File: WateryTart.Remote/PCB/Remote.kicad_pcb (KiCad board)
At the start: 2 copper layers, 41.3 x 112.4 mm, 26 parts, among them J1 Conn_01x04, J2 Conn_01x06, SW1 SW_Push, U1 lolin32_lite_V1.00

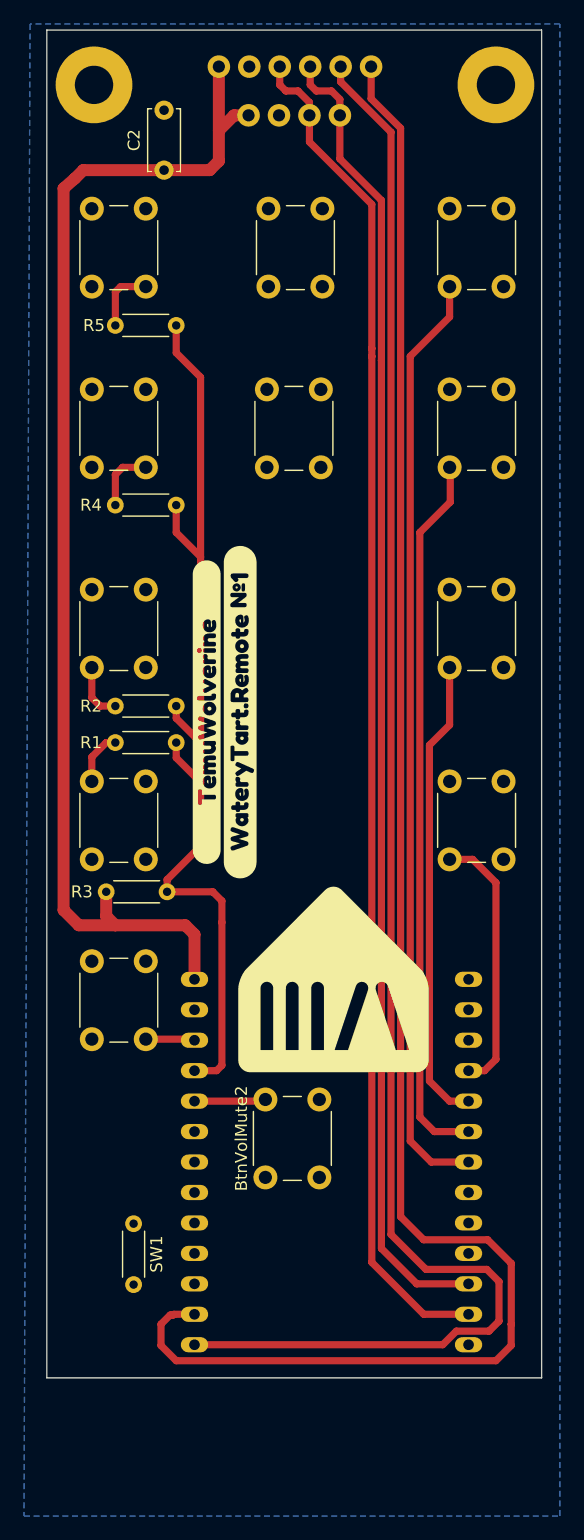
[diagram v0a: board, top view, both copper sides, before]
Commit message: Finalised schematic and pcb layout ready for first round of mfg
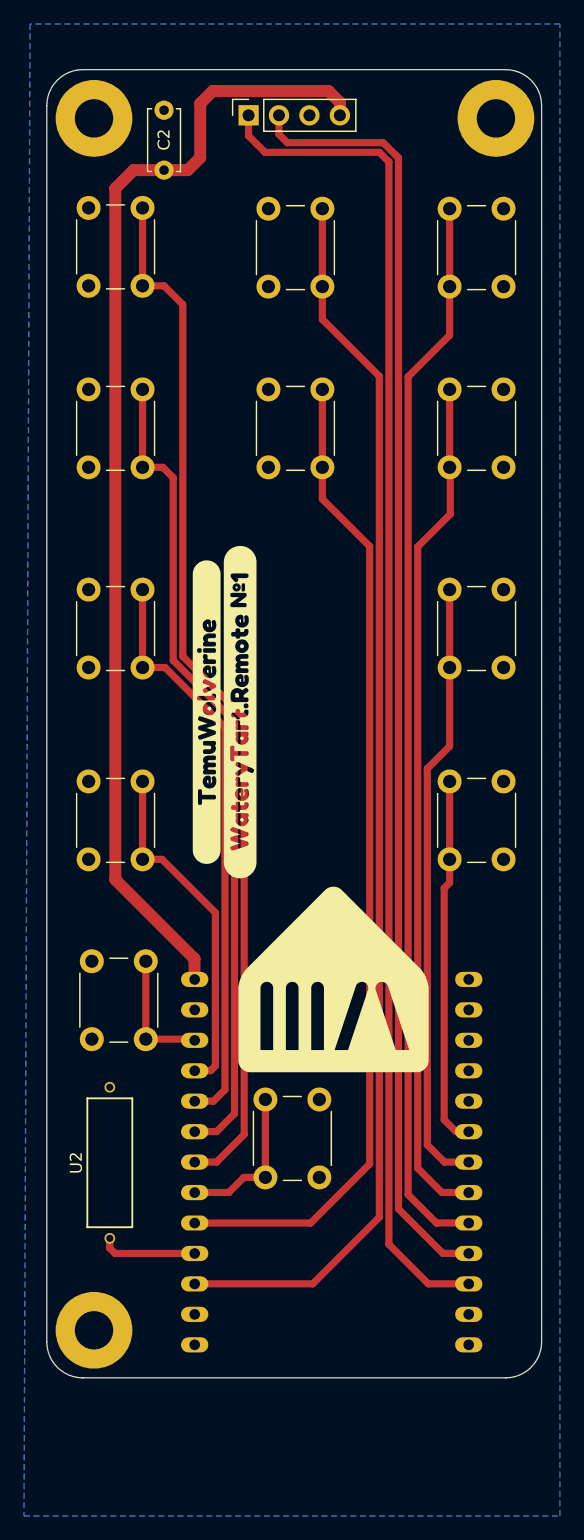
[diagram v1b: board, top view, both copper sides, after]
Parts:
- removed J2: Conn_01x06, PCM_SparkFun-Connector:1x06_P2.54mm
- removed R1: 220, Resistor_THT:R_Axial_DIN0204_L3.6mm_D1.6mm_P5.08mm_Horizontal
- removed R2: 4.7k, Resistor_THT:R_Axial_DIN0204_L3.6mm_D1.6mm_P5.08mm_Horizontal
- removed R3, R4: 10k, Resistor_THT:R_Axial_DIN0204_L3.6mm_D1.6mm_P5.08mm_Horizontal
- removed R5: 47k, Resistor_THT:R_Axial_DIN0204_L3.6mm_D1.6mm_P5.08mm_Horizontal
- removed SW1: SW_Push, Resistor_THT:R_Axial_DIN0204_L3.6mm_D1.6mm_P5.08mm_Horizontal
- added H3: MountingHole, MountingHole:MountingHole_3.2mm_M3_Pad, F.Cu at (122.7, 139.4)
- added U2: ~, EasyEDA_Lib:SW-TH_BD3.6-L10.6-LS12.6-D0.4, F.Cu at (124.0, 125.5)
- J1: footprint PCM_SparkFun-Connector:1x04_P2.54mm -> Connector_PinSocket_2.54mm:PinSocket_1x04_P2.54mm_Vertical
- U1: footprint PaulsCoolKicadLibrary:WEMOS_LOLIN32_LITE -> Paul:WEMOS_LOLIN32_LITE
- moved BtnVolDown1 8.06 mm to (122.2, 100.2), turned to 90 degrees
- moved BtnVolUp1 8.06 mm to (122.2, 84.2), turned to 90 degrees
- moved BtnPreviousTrack1 7.81 mm to (126.7, 45.8), turned to -90 degrees
- moved BtnCycleRepeat1 7.76 mm to (126.7, 61.0), turned to -90 degrees
- moved H1 2.79 mm to (122.7, 38.4)
- moved H2 2.79 mm to (156.2, 38.4)
- moved BtnFavourite1 0.13 mm to (137.2, 67.5)
- turned J1 to 90 degrees
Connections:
- BtnCycleRepeat1 pad 1: GND -> repeat
- BtnCycleRepeat1 pad 2: /sRepeat -> GND
- BtnPreviousTrack1 pad 1: GND -> previoustrack
- BtnPreviousTrack1 pad 2: /sPreviousTrack -> GND
- BtnVolDown1 pad 2: /sVolDown -> voldown
- BtnVolUp1 pad 2: /sVolUp -> volup
- J1 pad 1: +3.3V -> display_SDA
- J1 pad 2: GND -> display_sck
- J1 pad 3: display_sck/SDI -> GND
- J1 pad 4: display_SDA/SCLK -> +3.3V
- U1 pad 10: unconnected-(U1-27-Pad10) -> display_sck
- U1 pad 11: display_SDA/SCLK -> display_SDA
- U1 pad 12: display_sck/SDI -> unconnected-(U1-Pad12)
- U1 pad 14: display_DC -> unconnected-(U1-13-Pad14)
- U1 pad 15: display_CS -> unconnected-(U1-Pad15)
- U1 pad 16: unconnected-(U1-2-Pad16) -> playpause
- U1 pad 17: unconnected-(U1-0-Pad17) -> /wakeup
- U1 pad 18: unconnected-(U1-4-Pad18) -> Favourite
- U1 pad 19: unconnected-(U1-16-Pad19) -> misc
- U1 pad 20: unconnected-(U1-17-Pad20) -> previoustrack
- U1 pad 21: unconnected-(U1-5-Pad21) -> repeat
- U1 pad 22: misc -> volup
- U1 pad 23: switch_readout -> voldown
- U1 pad 4: playerprevious -> unconnected-(U1-34-Pad4)
- U1 pad 5: playernext -> unconnected-(U1-35-Pad5)
- U1 pad 6: Shuffle -> playerprevious
- U1 pad 7: nexttrack -> playernext
- U1 pad 8: unconnected-(U1-25-Pad8) -> Shuffle
- U1 pad 9: unconnected-(U1-26-Pad9) -> nexttrack
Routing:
- net display_CS: track 149.8 -> 0.00 mm
- net display_DC: track 139.3 -> 0.00 mm
- net display_sck/SDI: track 113.4 -> 0.00 mm
- net display_SDA: track 0.00 -> 112.6 mm
- net display_SDA/SCLK: track 110.3 -> 0.00 mm
- net display_sck: track 0.00 -> 107.4 mm
- net playpause: track 0.00 -> 103.8 mm
- net previoustrack: track 0.00 -> 86.9 mm
- net switch_readout: track 83.5 -> 0.00 mm
- net Favourite: track 0.00 -> 82.9 mm
- net repeat: track 0.00 -> 68.5 mm
- net volup: track 0.00 -> 48.6 mm
- net voldown: track 0.00 -> 29.1 mm
- net playernext: track 39.1 -> 51.1 mm
- net nexttrack: track 78.2 -> 89.7 mm
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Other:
- board size 41.3 x 112.4 mm -> 41.3 x 109.1 mm
